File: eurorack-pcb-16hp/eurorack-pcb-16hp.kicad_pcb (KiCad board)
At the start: 2 copper layers, 69.3 x 108.3 mm, 0 parts

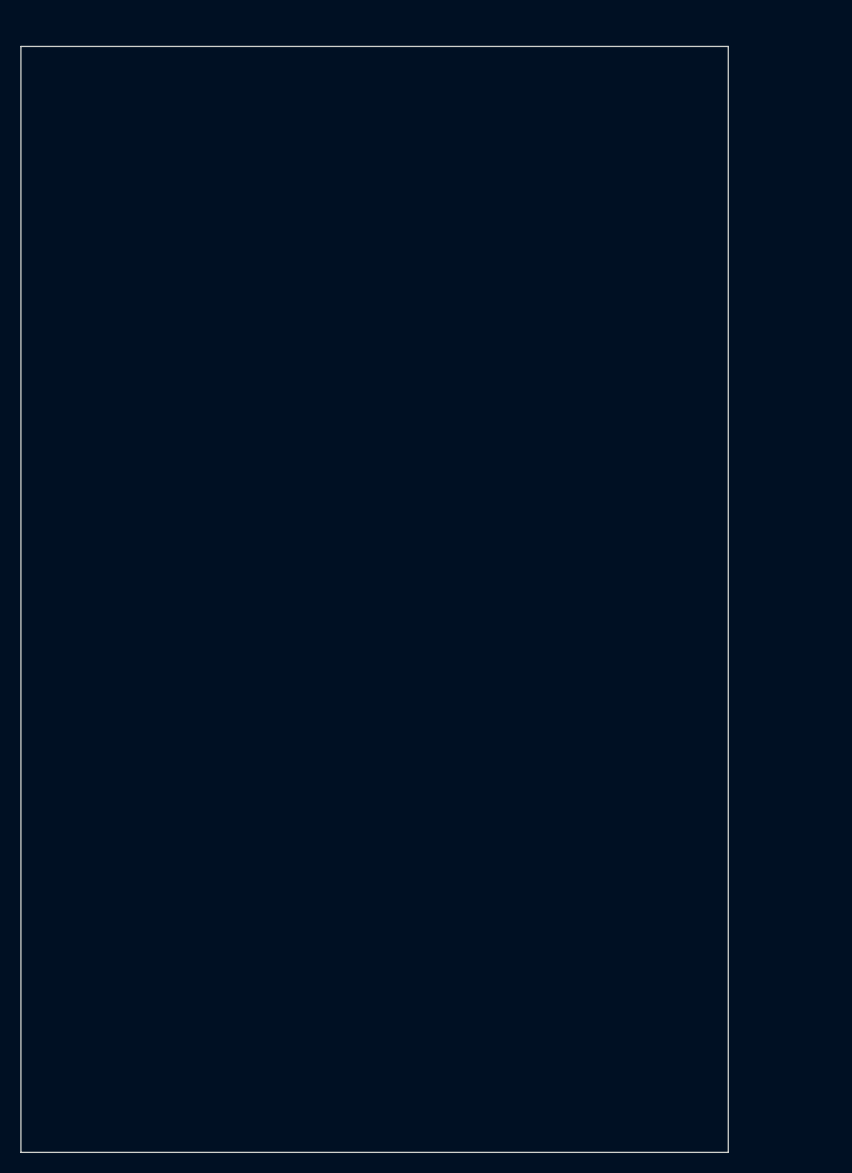
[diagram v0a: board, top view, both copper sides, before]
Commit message: Minor adjustments to PCB positioning. Moving everything into a single folder to be easier for kiCad to pick up all templates from user-template path
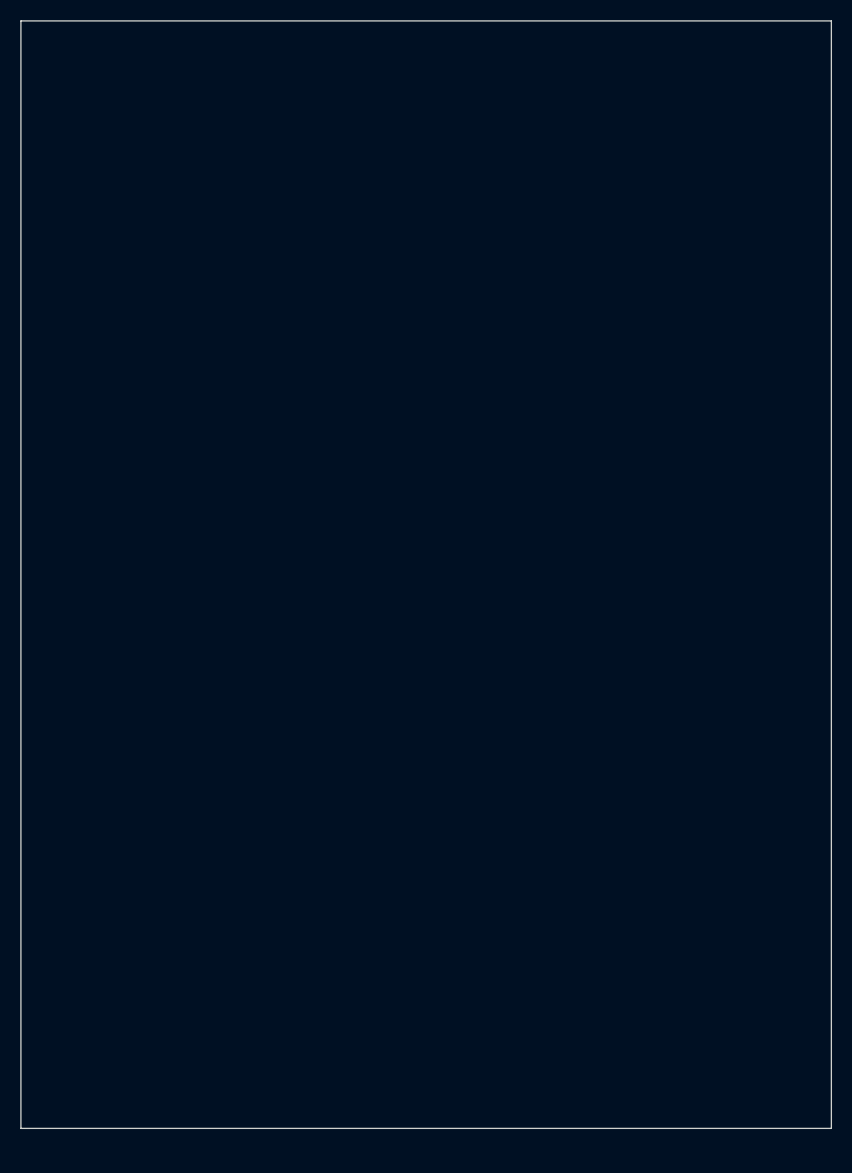
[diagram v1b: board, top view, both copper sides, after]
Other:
- board size 69.3 x 108.3 mm -> 79.4 x 108.5 mm
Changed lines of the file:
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@@
   )
   (net 0 "")
-  (gr_line (start 0.75 12.5) (end 0.75 120.85) (layer "Edge.Cuts") (width 0.1))
-  (gr_line (start 70.05 120.85) (end 70.05 12.5) (layer "Edge.Cuts") (width 0.1))
-  (gr_line (start 0.75 120.85) (end 70.05 120.85) (layer "Edge.Cuts") (width 0.1))
-  (gr_line (start 0.75 12.5) (end 70.05 12.5) (layer "Edge.Cuts") (width 0.1))
-  (gr_line (start 70.8 0) (end 70.8 128.5) (layer "User.1") (width 0.1))
+  (gr_line (start 0.75 10) (end 0.75 118.5) (layer "Edge.Cuts") (width 0.1))
+  (gr_line (start 80.15 118.5) (end 80.15 10) (layer "Edge.Cuts") (width 0.1))
+  (gr_line (start 0.75 118.5) (end 80.15 118.5) (layer "Edge.Cuts") (width 0.1))
+  (gr_line (start 0.75 10) (end 80.15 10) (layer "Edge.Cuts") (width 0.1))
+  (gr_line (start 80.9 0) (end 80.9 128.5) (layer "User.1") (width 0.1))
   (gr_line (start 0 128.5) (end 0 0) (layer "User.1") (width 0.1))
-  (gr_line (start 0 0) (end 70.8 0) (layer "User.1") (width 0.1))
-  (gr_line (start 70.8 128.5) (end 0 128.5) (layer "User.1") (width 0.1))
+  (gr_line (start 0 0) (end 80.9 0) (layer "User.1") (width 0.1))
+  (gr_line (start 80.9 128.5) (end 0 128.5) (layer "User.1") (width 0.1))
 )
